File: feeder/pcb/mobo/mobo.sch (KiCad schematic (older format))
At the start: 25 parts, among them J1 SERIAL_BRIDGE, J2 Spring_Finger_Interface, J3 AVR-ISP-6, M1 Motor_DC, SW1 SW_Push, SW2 SW_Push, SW3 SW_Push, SW4 SW_SPDT, U1 ATmega328-AU, U2 VCNT2020, U3 DRV8838, Y1 Resonator_Small

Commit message: first commit for stm32 feeder!
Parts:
- removed C1: 10uF, Capacitor_SMD:C_0805_2012Metric, symbol Device:CP1_Small
- removed C2: 0.1uF, Capacitor_SMD:C_0805_2012Metric, symbol Device:C_Small
- removed D2: LED2, LED_SMD:LED_0805_2012Metric, symbol Device:LED
- removed J3: AVR-ISP-6, Connector_PinHeader_2.54mm:PinHeader_2x03_P2.54mm_Vertical, symbol Connector:AVR-ISP-6
- removed R4: 470R, Resistor_SMD:R_0805_2012Metric_Pad1.15x1.40mm_HandSolder, symbol Device:R_Small
- removed R7: 10K, Resistor_SMD:R_0805_2012Metric_Pad1.15x1.40mm_HandSolder, symbol Device:R_Small
- removed U1: ATmega328-AU, Package_QFP:TQFP-32_7x7mm_P0.8mm, symbol MCU_Microchip_ATmega:ATmega328-AU
- removed U3: DRV8838, Package_SON:WSON-8-1EP_2x2mm_P0.5mm_EP0.9x1.6mm_ThermalVias, symbol stephen:DRV8838
- removed Y1: Resonator_Small, Crystal:Resonator_SMD_muRata_CSTxExxV-3Pin_3.0x1.1mm, symbol Device:Resonator_Small
- added C? (x2): 10pF, Capacitor_SMD:C_0805_2012Metric, symbol Device:C_Small
- added C?: 0.1uF, Capacitor_SMD:C_0805_2012Metric, symbol Device:C_Small
- added C?: 4.7uF, Capacitor_SMD:C_0805_2012Metric, symbol Device:C_Small
- added C?: 2.2uF, Capacitor_SMD:C_0805_2012Metric, symbol Device:C_Small
- added C?: 10uF, Capacitor_SMD:C_0805_2012Metric, symbol Device:C_Small
- added D?: LED1, LED_SMD:LED_0805_2012Metric, symbol Device:LED
- added J?: Conn_ARM_JTAG_SWD_10, symbol Connector:Conn_ARM_JTAG_SWD_10
- added M?: PEEL_MOTOR, Connector_PinHeader_2.54mm:PinHeader_1x02_P2.54mm_Vertical, symbol Motor:Motor_DC
- added R?: R_Small, symbol Device:R_Small
- added R?: 470R, Resistor_SMD:R_0805_2012Metric_Pad1.15x1.40mm_HandSolder, symbol Device:R_Small
- added U?: DRV8833PW, Package_SO:TSSOP-16_4.4x5mm_P0.65mm, symbol Driver_Motor:DRV8833PW
- added U?: MAX3485, symbol Interface_UART:MAX3485
- added U?: STM32F030K6Tx, Package_QFP:LQFP-32_7x7mm_P0.8mm, symbol MCU_ST_STM32F0:STM32F030K6Tx
- added Y?: 8MHz, symbol Device:Crystal_Small
- C5: value 0.1uF -> 0.01uF
- M1: value Motor_DC -> DRIVE_MOTOR
- SW1: value SW_Push -> BUTTON_1
- SW2: value SW_Push -> BUTTON_2
- SW3: value SW_Push -> RESET_BUTTON
- SW4: value SW_SPDT -> TAPE_DETECT
- U2: symbol stephen:VCNT2020 -> mobo-rescue:VCNT2020-stephen
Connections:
- net labels added: +3V3, DRIVE1, DRIVE2, FILM_TENSION, LED2, MCU_RX, MCU_TX, PEEL1, PEEL2, RS-485+, RS-485-, RTS, SLOT_DETECT, SWCLK, SWDIO, TAPE_DETECT
- net labels removed: 22, EN, LIMIT, MISO, MOSI, PH, RST, SCK, SCL, SDA, nSLEEP
- wire segments 80 -> 97
- no-connect marks 0 -> 3
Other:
- moved on the sheet: C3, C4, C5, D1, J1, JP1, M1, R3, R5, R6, SW1, SW2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

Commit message: added footprint for limit switch
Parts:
- added C? (x2): 10uF, Capacitor_SMD:C_0805_2012Metric, symbol Device:C_Small
- added U?: AP1117-33, Package_TO_SOT_SMD:SOT-223-3_TabPin2, symbol Regulator_Linear:AP1117-33
- J3: renamed from J?; value Conn_ARM_JTAG_SWD_10 -> SWD_10; footprint (none) -> Connector_PinHeader_2.00mm:PinHeader_2x05_P2.00mm_Vertical_SMD; symbol Connector:Conn_ARM_JTAG_SWD_10 -> mobo-rescue:Conn_ARM_JTAG_SWD_10-Connector
- R2: renamed from R?; footprint (none) -> Resistor_SMD:R_0805_2012Metric
- U3: renamed from U?; footprint (none) -> Package_SO:SO-8_5.3x6.2mm_P1.27mm
- Y1: renamed from Y?; footprint (none) -> Crystal:Crystal_SMD_3225-4Pin_3.2x2.5mm_HandSoldering
- gave numbers to parts that had none: 11
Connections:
- net labels added: RESET
- wire segments 97 -> 110
- no-connect marks 3 -> 5
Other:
- note added: "I/O"
- note added: "MCU"
- note added: "MOTOR CONTROL"
- note added: "POWER"
- moved on the sheet: C1, C2, C3, C4, C5, C6, C7, C8, C9, D1, D2, J1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

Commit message: started layout
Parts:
- removed J1: SERIAL_BRIDGE, Connector_PinHeader_2.54mm:PinHeader_1x06_P2.54mm_Vertical, symbol Connector:Conn_01x06_Female
- removed J2: Spring_Finger_Interface, stephen:springFingerContactPads_4x, symbol Connector:Conn_01x04_Male
- added C12: 0.01uF, Capacitor_SMD:C_0805_2012Metric, symbol Device:C_Small
- added C13: 1uF, Capacitor_SMD:C_0805_2012Metric, symbol Device:C_Small
- added J1: Conn_01x05_Male, symbol Connector:Conn_01x05_Male
- added JP2: FILM_TENSION, Jumper:SolderJumper-2_P1.3mm_Open_RoundedPad1.0x1.5mm, symbol Device:Jumper_NO_Small
- added R4: ?, Resistor_SMD:R_0805_2012Metric, symbol Device:R_Small
- added SW5: FILM_TENSION, index:K5-1624SA-01, symbol Switch:SW_SPDT
- added TP1: MCU_TX, TestPoint:TestPoint_Pad_D2.0mm, symbol stephen:TEST
- added TP2: MCU_RX, TestPoint:TestPoint_Pad_D2.0mm, symbol stephen:TEST
- gave numbers to parts that had none: 3
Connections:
- net labels removed: DTR, RX, TX
- wire segments 110 -> 121

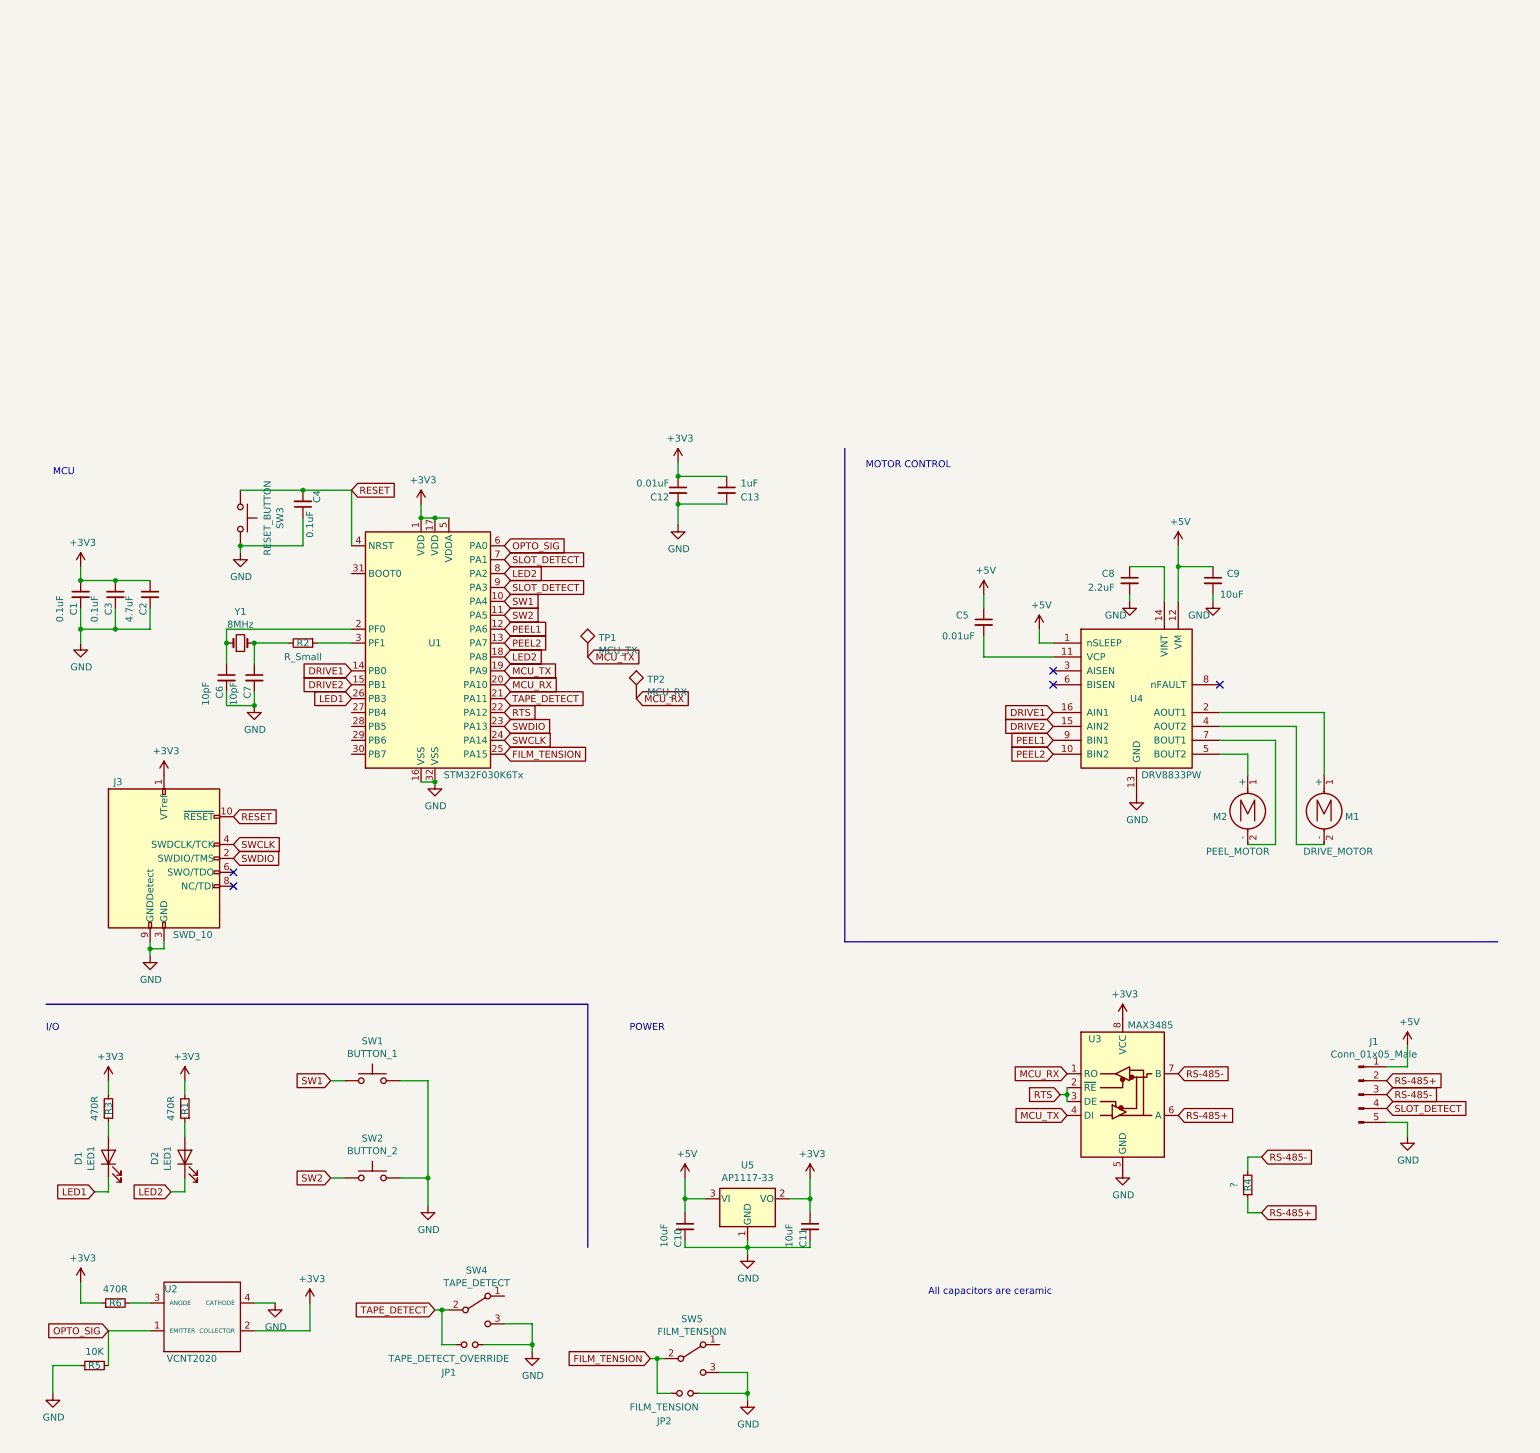
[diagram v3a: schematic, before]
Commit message: added test points for rx, tx, 3v3, 5v, and gnd. cleaned up schematic layout
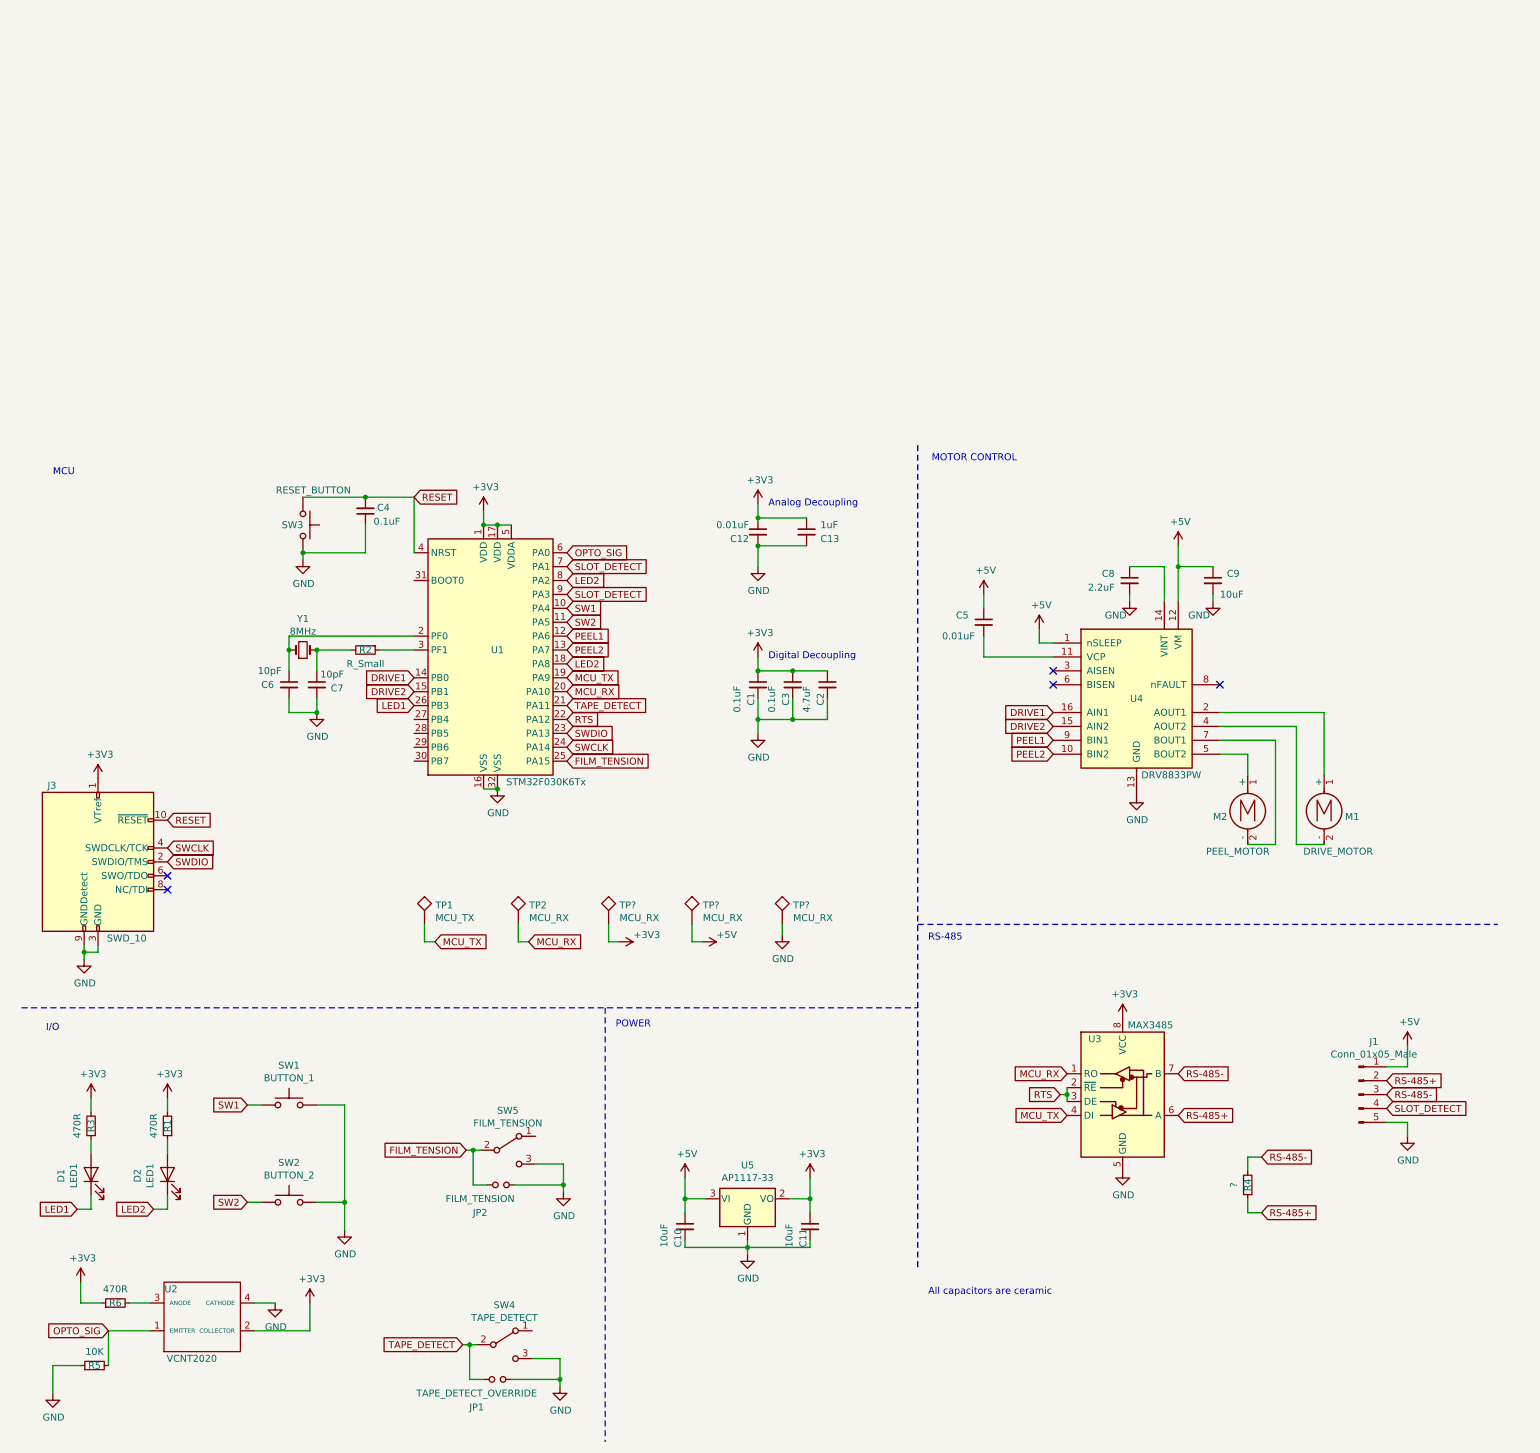
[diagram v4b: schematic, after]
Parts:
- added TP? (x3): MCU_RX, TestPoint:TestPoint_Pad_D2.0mm, symbol stephen:TEST
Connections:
- net +3V3: now also TP?.1
- net +5V: now also TP?.1
- net GND: now also TP?.1
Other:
- note added: "Analog Decoupling"
- note added: "Digital Decoupling"
- note added: "RS-485"
- moved on the sheet: C1, C12, C13, C2, C3, C4, C6, C7, D1, D2, J3, JP1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

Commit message: starting layout for feeder
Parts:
- removed Y1: 8MHz, Crystal:Crystal_SMD_3225-4Pin_3.2x2.5mm_HandSoldering, symbol Device:Crystal_Small
- added Y1: Crystal_GND24_Small, Crystal:Crystal_SMD_3225-4Pin_3.2x2.5mm_HandSoldering, symbol Device:Crystal_GND24_Small
- J1: value Conn_01x05_Male -> SPRING_FINGER_INTERFACE; footprint (none) -> index:5-pad-spring-finger-interface
- R4: value ? -> 120R
- SW4: footprint stephen:MDS6500AL02SR -> index:K5-1624SA-01
- gave numbers to parts that had none: 3
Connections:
- net GND: now also Y1.2, Y1.4
- net at C6.1, U1.2 (PF0): now also Y1.1
- net at C7.1, R2.2: now also Y1.3
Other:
- note added: "All capacitors are ceramic\nAt least 16V tolerant\n"
- note removed: "All capacitors are ceramic\n"
- moved on the sheet: J1, R4
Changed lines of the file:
@@
 F 0 "SW4" H 4000 7335 50  0000 C CNN
 F 1 "TAPE_DETECT" H 4000 7244 50  0000 C CNN
-F 2 "stephen:MDS6500AL02SR" H 4000 7050 50  0001 C CNN
+F 2 "index:K5-1624SA-01" H 4000 7050 50  0001 C CNN
 F 3 "" H 4000 7050 50  0001 C CNN
 	1    4000 7050
@@
 L power:+5V #PWR0101
 U 1 1 5DC9F070
-P 10500 4900
-F 0 "#PWR0101" H 10500 4750 50  0001 C CNN
-F 1 "+5V" H 10515 5073 50  0000 C CNN
-F 2 "" H 10500 4900 50  0001 C CNN
-F 3 "" H 10500 4900 50  0001 C CNN
-	1    10500 4900
+P 10500 4550
+F 0 "#PWR0101" H 10500 4400 50  0001 C CNN
+F 1 "+5V" H 10515 4723 50  0000 C CNN
+F 2 "" H 10500 4550 50  0001 C CNN
+F 3 "" H 10500 4550 50  0001 C CNN
+	1    10500 4550
 	1    0    0    -1
 $EndComp
@@
 L power:GND #PWR0102
 U 1 1 5DC9F0F0
-P 10500 5550
-F 0 "#PWR0102" H 10500 5300 50  0001 C CNN
-F 1 "GND" H 10505 5377 50  0000 C CNN
-F 2 "" H 10500 5550 50  0001 C CNN
-F 3 "" H 10500 5550 50  0001 C CNN
-	1    10500 5550
-	1    0    0    -1
-$EndComp
-Wire Wire Line
-	10350 5450 10500 5450
-Wire Wire Line
-	10500 5450 10500 5550
-Wire Wire Line
-	10350 5050 10500 5050
-Wire Wire Line
-	10500 5050 10500 4900
-Text GLabel 10350 5150 2    50   Input ~ 0
+P 10500 5200
+F 0 "#PWR0102" H 10500 4950 50  0001 C CNN
+F 1 "GND" H 10505 5027 50  0000 C CNN
+F 2 "" H 10500 5200 50  0001 C CNN
+F 3 "" H 10500 5200 50  0001 C CNN
+	1    10500 5200
+	1    0    0    -1
+$EndComp
+Wire Wire Line
+	10350 5100 10500 5100
+Wire Wire Line
+	10500 5100 10500 5200
+Wire Wire Line
+	10350 4700 10500 4700
+Wire Wire Line
+	10500 4700 10500 4550
+Text GLabel 10350 4800 2    50   Input ~ 0
 RS-485+
-Text GLabel 10350 5250 2    50   Input ~ 0
+Text GLabel 10350 4900 2    50   Input ~ 0
 RS-485-
 $Comp
@@
 Wire Wire Line
 	1025 5375 1025 5275
-Text Notes 7050 6700 0    50   ~ 0
-All capacitors are ceramic\n
+Text Notes 7050 6750 0    50   ~ 0
+All capacitors are ceramic\nAt least 16V tolerant\n
 $Comp
 L power:GND #PWR0133
@@
 $EndComp
 $Comp
-L Device:Crystal_Small Y1
-U 1 1 5F61897D
-P 2550 2050
-F 0 "Y1" H 2550 2275 50  0000 C CNN
-F 1 "8MHz" H 2550 2184 50  0000 C CNN
-F 2 "Crystal:Crystal_SMD_3225-4Pin_3.2x2.5mm_HandSoldering" H 2550 2050 50  0001 C CNN
-F 3 "~" H 2550 2050 50  0001 C CNN
-	1    2550 2050
-	1    0    0    -1
-$EndComp
-$Comp
 L Device:C_Small C6
 U 1 1 5F61983F
@@
 	3350 1950 2450 1950
 Wire Wire Line
-	2450 1950 2450 2050
-Wire Wire Line
-	2450 2200 2450 2050
-Connection ~ 2450 2050
-Wire Wire Line
 	2650 2200 2650 2050
-Connection ~ 2650 2050
 $Comp
 L power:GND #PWR0109
@@
 	2650 2500 2650 2400
 Wire Wire Line
-	2650 2500 2450 2500
+	2650 2500 2550 2500
 Wire Wire Line
 	2450 2500 2450 2400
@@
 Text GLabel 4450 1650 2    50   Input ~ 0
 SLOT_DETECT
-Text GLabel 10350 5350 2    50   Input ~ 0
+Text GLabel 10350 5000 2    50   Input ~ 0
 SLOT_DETECT
 Text GLabel 1575 3575 2    50   Input ~ 0
@@
 U 1 1 5F66C4A6
 P 5300 6200
-F 0 "C10" V 5250 6050 50  0000 L CNN
-F 1 "10uF" V 5150 6050 50  0000 L CNN
+F 0 "C10" H 5100 6100 50  0000 L CNN
+F 1 "10uF" H 5075 6275 50  0000 L CNN
 F 2 "Capacitor_SMD:C_0805_2012Metric" H 5300 6200 50  0001 C CNN
 F 3 "~" H 5300 6200 50  0001 C CNN
@@
 U 1 1 5F66CF41
 P 6200 6200
-F 0 "C11" V 6150 6050 50  0000 L CNN
-F 1 "10uF" V 6050 6050 50  0000 L CNN
+F 0 "C11" H 6250 6100 50  0000 L CNN
+F 1 "10uF" H 6225 6275 50  0000 L CNN
 F 2 "Capacitor_SMD:C_0805_2012Metric" H 6200 6200 50  0001 C CNN
 F 3 "~" H 6200 6200 50  0001 C CNN
@@
 L Device:R_Small R4
 U 1 1 5F6B917D
-P 9350 5900
-F 0 "R4" V 9350 5900 50  0000 C CNN
-F 1 "?" V 9450 5900 50  0000 C CNN
-F 2 "Resistor_SMD:R_0805_2012Metric" H 9350 5900 50  0001 C CNN
-F 3 "~" H 9350 5900 50  0001 C CNN
-	1    9350 5900
+P 9700 5875
+F 0 "R4" H 9600 5875 50  0000 C CNN
+F 1 "120R" H 9875 5875 50  0000 C CNN
+F 2 "Resistor_SMD:R_0805_2012Metric" H 9700 5875 50  0001 C CNN
+F 3 "~" H 9700 5875 50  0001 C CNN
+	1    9700 5875
 	-1   0    0    1
 $EndComp
-Text GLabel 9450 6100 2    50   Input ~ 0
+Text GLabel 9800 6075 2    50   Input ~ 0
 RS-485+
-Text GLabel 9450 5700 2    50   Input ~ 0
+Text GLabel 9800 5675 2    50   Input ~ 0
 RS-485-
 Wire Wire Line
-	9450 6100 9350 6100
-Wire Wire Line
-	9350 6100 9350 6000
-Wire Wire Line
-	9350 5800 9350 5700
-Wire Wire Line
-	9350 5700 9450 5700
+	9800 6075 9700 6075
+Wire Wire Line
+	9700 6075 9700 5975
+Wire Wire Line
+	9700 5775 9700 5675
+Wire Wire Line
+	9700 5675 9800 5675
 Text GLabel 8050 5400 0    50   Input ~ 0
 MCU_TX
@@
 L Connector:Conn_01x05_Male J1
 U 1 1 5F6CB070
-P 10150 5250
-F 0 "J1" H 10258 5631 50  0000 C CNN
-F 1 "Conn_01x05_Male" H 10258 5540 50  0000 C CNN
-F 2 "" H 10150 5250 50  0001 C CNN
-F 3 "~" H 10150 5250 50  0001 C CNN
-	1    10150 5250
+P 10150 4900
+F 0 "J1" H 10050 4925 50  0000 C CNN
+F 1 "SPRING_FINGER_INTERFACE" H 9950 5200 50  0000 C CNN
+F 2 "index:5-pad-spring-finger-interface" H 10150 4900 50  0001 C CNN
+F 3 "~" H 10150 4900 50  0001 C CNN
+	1    10150 4900
 	1    0    0    -1
 $EndComp
@@
 	4100 4150 4175 4150
 $Comp
-L stephen:TEST TP?
+L stephen:TEST TP3
 U 1 1 5F789B2A
 P 4750 4025
-F 0 "TP?" H 4828 4163 50  0000 L CNN
+F 0 "TP3" H 4828 4163 50  0000 L CNN
 F 1 "MCU_RX" H 4828 4072 50  0000 L CNN
 F 2 "TestPoint:TestPoint_Pad_D2.0mm" H 4750 4025 50  0001 C CNN
@@
 $EndComp
 $Comp
-L stephen:TEST TP?
+L stephen:TEST TP4
 U 1 1 5F789C99
 P 5350 4025
-F 0 "TP?" H 5428 4163 50  0000 L CNN
+F 0 "TP4" H 5428 4163 50  0000 L CNN
 F 1 "MCU_RX" H 5428 4072 50  0000 L CNN
 F 2 "TestPoint:TestPoint_Pad_D2.0mm" H 5350 4025 50  0001 C CNN
@@
 $EndComp
 $Comp
-L stephen:TEST TP?
+L stephen:TEST TP5
 U 1 1 5F78A07B
 P 6000 4025
-F 0 "TP?" H 6078 4163 50  0000 L CNN
+F 0 "TP5" H 6078 4163 50  0000 L CNN
 F 1 "MCU_RX" H 6078 4072 50  0000 L CNN
 F 2 "TestPoint:TestPoint_Pad_D2.0mm" H 6000 4025 50  0001 C CNN
@@
 $EndComp
 $Comp
-L power:+3V3 #PWR?
+L power:+3V3 #PWR0132
 U 1 1 5F78A353
 P 4825 4150
-F 0 "#PWR?" H 4825 4000 50  0001 C CNN
+F 0 "#PWR0132" H 4825 4000 50  0001 C CNN
 F 1 "+3V3" V 4775 4350 50  0000 C CNN
 F 2 "" H 4825 4150 50  0001 C CNN
@@
 $EndComp
 $Comp
-L power:GND #PWR?
+L power:GND #PWR0134
 U 1 1 5F78A650
 P 6000 4100
-F 0 "#PWR?" H 6000 3850 50  0001 C CNN
+F 0 "#PWR0134" H 6000 3850 50  0001 C CNN
 F 1 "GND" H 6005 3927 50  0000 C CNN
 F 2 "" H 6000 4100 50  0001 C CNN
@@
 $EndComp
 $Comp
-L power:+5V #PWR?
+L power:+5V #PWR0135
 U 1 1 5F78A7EE
 P 5425 4150
-F 0 "#PWR?" H 5425 4000 50  0001 C CNN
+F 0 "#PWR0135" H 5425 4000 50  0001 C CNN
 F 1 "+5V" V 5375 4325 50  0000 C CNN
 F 2 "" H 5425 4150 50  0001 C CNN
@@
 Wire Wire Line
 	4750 4150 4825 4150
+$Comp
+L Device:Crystal_GND24_Small Y1
+U 1 1 5F7F9F70
+P 2550 2050
+F 0 "Y1" H 2694 2096 50  0000 L CNN
+F 1 "Crystal_GND24_Small" H 2694 2005 50  0000 L CNN
+F 2 "Crystal:Crystal_SMD_3225-4Pin_3.2x2.5mm_HandSoldering" H 2550 2050 50  0001 C CNN
+F 3 "~" H 2550 2050 50  0001 C CNN
+	1    2550 2050
+	1    0    0    -1
+$EndComp
+Wire Wire Line
+	2450 1950 2450 2050
+Connection ~ 2450 2050
+Wire Wire Line
+	2450 2050 2450 2200
+Connection ~ 2650 2050
+Wire Wire Line
+	2550 2175 2550 2500
+Connection ~ 2550 2500
+Wire Wire Line
+	2550 2500 2450 2500
+Wire Wire Line
+	2175 2500 2450 2500
+Connection ~ 2450 2500
+Wire Wire Line
+	2175 1850 2550 1850
+Wire Wire Line
+	2550 1850 2550 1925
+Wire Wire Line
+	2175 1850 2175 2500
 $EndSCHEMATC
